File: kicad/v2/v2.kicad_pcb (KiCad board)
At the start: 2 copper layers, 314.8 x 118.8 mm, 114 parts, among them U1 Raspberry_Pi_Pico, U2 Raspberry_Pi_Pico

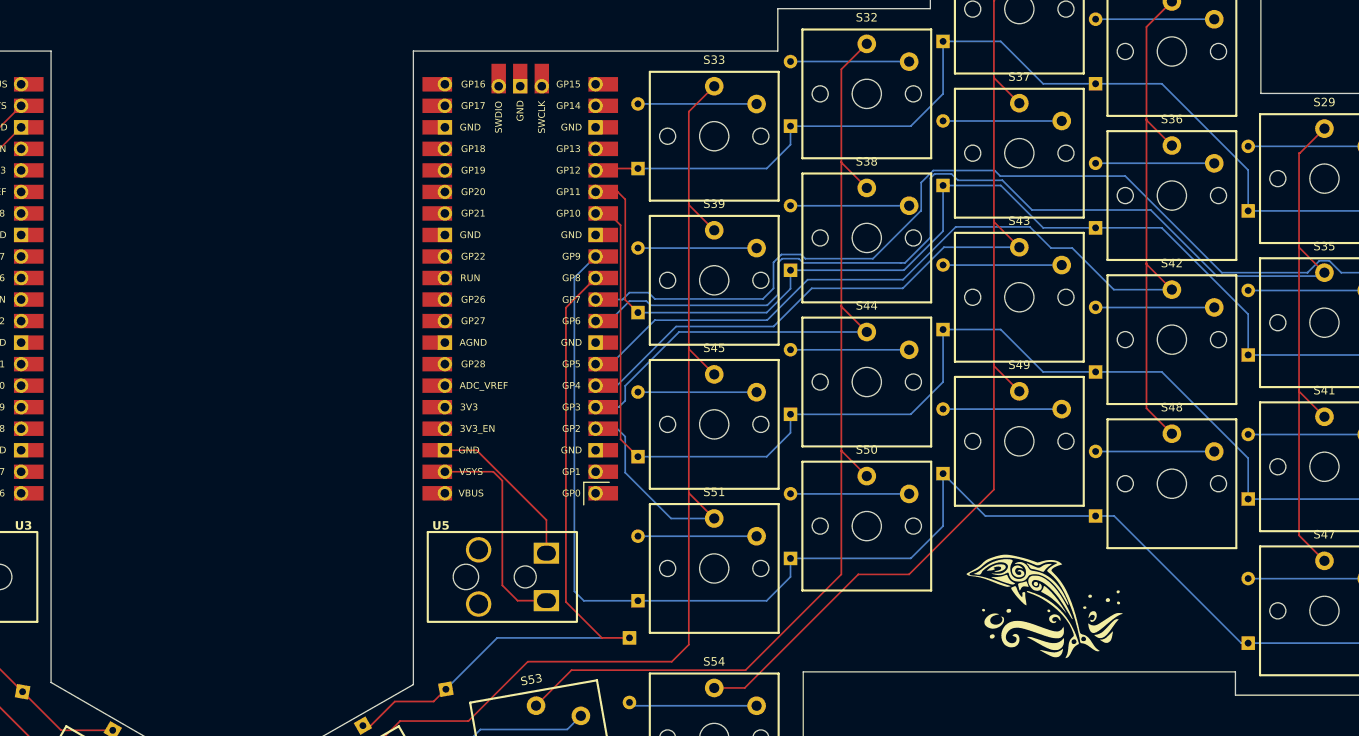
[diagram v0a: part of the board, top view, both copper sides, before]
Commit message: add: second stability beam
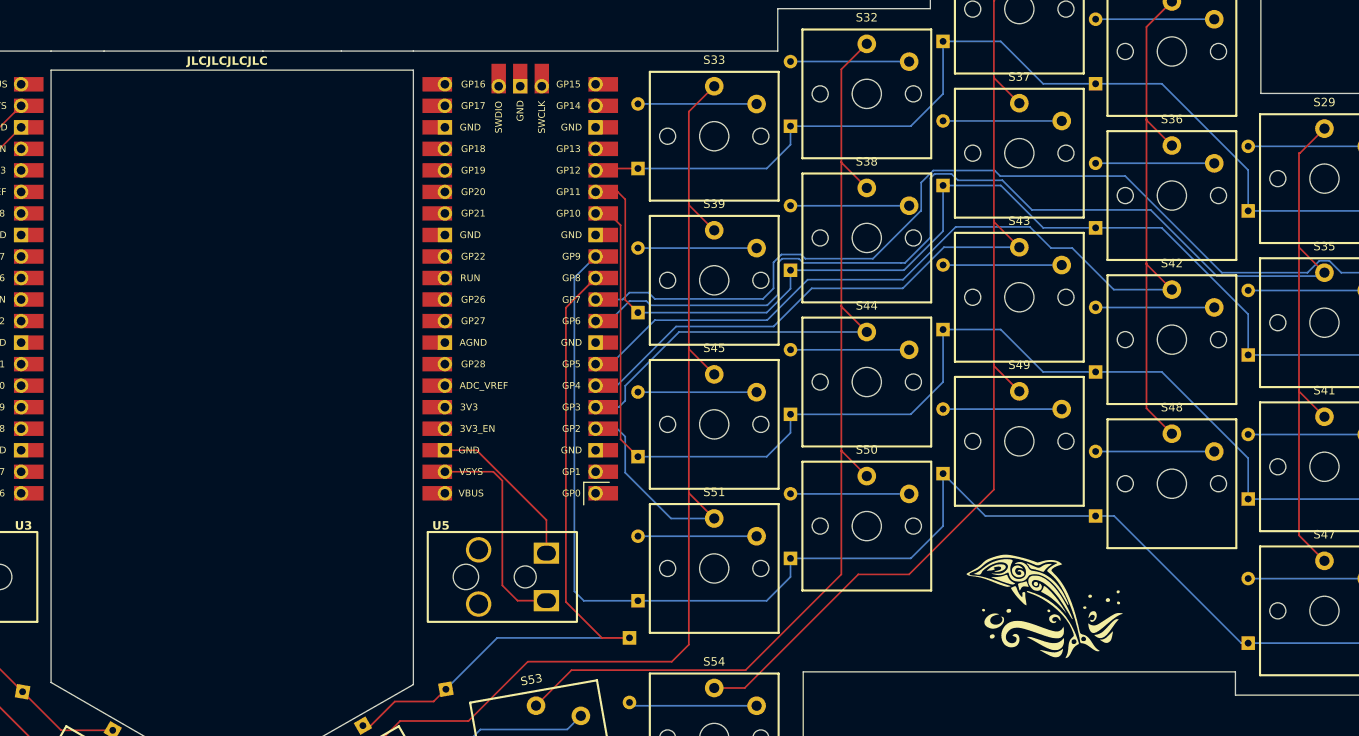
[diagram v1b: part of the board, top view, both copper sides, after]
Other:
- outline, holes or cut-outs redrawn
- board text added: "JLCJLCJLCJLC"
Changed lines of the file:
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@@
 			(xy 248 193.75) (xy 267.5 193.75) (xy 267.5 176) (xy 318.5 176) (xy 318.5 178.75) (xy 357.5 178.75)
 			(xy 357.5 107.75) (xy 321.5 107.75) (xy 321.5 92.75) (xy 303.5 92.75) (xy 303.5 87.75) (xy 282.5 87.75)
-			(xy 282.5 97.75) (xy 264.5 97.75) (xy 264.5 102.75) (xy 221.5 102.75) (xy 221.5 177.5) (xy 204 187.5)
-			(xy 196.5 187.5) (xy 178.75 177.25) (xy 178.75 102.75) (xy 135.75 102.75) (xy 135.75 97.75) (xy 117.75 97.75)
+			(xy 282.5 97.75) (xy 264.5 97.75) (xy 264.5 102.75) (xy 221.5 102.75) (xy 213 102.75) (xy 203.75 102.75)
+			(xy 196.25 102.75) (xy 185 102.75) (xy 178.75 102.75) (xy 135.75 102.75) (xy 135.75 97.75) (xy 117.75 97.75)
 			(xy 117.75 87.75) (xy 96.75 87.75) (xy 96.75 92.75) (xy 78.75 92.75) (xy 78.75 107.75) (xy 42.75 107.75)
 		)
@@
 		(layer "Edge.Cuts")
 	)
+	(gr_poly
+		(pts
+			(xy 178.75 105) (xy 221.5 105) (xy 221.5 177.5) (xy 204 187.5) (xy 196.5 187.5) (xy 178.75 177.25)
+		)
+		(stroke
+			(width 0.05)
+			(type solid)
+		)
+		(fill none)
+		(layer "Edge.Cuts")
+	)
 	(gr_text "Splashboard made with <3 by Flo "
 		(at 312.84 173.95 0)
@@
 		)
 	)
+	(gr_text "JLCJLCJLCJLC"
+		(at 194.75 104.5 0)
+		(layer "F.SilkS")
+		(effects
+			(font
+				(size 1 1)
+				(thickness 0.2)
+				(bold yes)
+			)
+			(justify left bottom)
+		)
+	)
 	(segment
 		(start 154 130.25)
@@
 		(width 0.2)
 		(layer "B.Cu")
-		(net 108)
-	)
-	(segment
-		(start 327 128.9)
-		(end 327.020101 128.9)
-		(width 0.2)
-		(layer "B.Cu")
